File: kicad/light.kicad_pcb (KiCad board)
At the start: 2 copper layers, 166 parts, among them J1 USB_C, J2 SM03B-SRSS-TB, J3 Barrell Jack, J4 01x04, J5 Conn_01x09_MountingPin, J6 01x04, SW1 Boot, SW2 Reset, SW3 On/Off, SW4 Mode, SW5 RotaryEncoder_Switch_MP, U1 RP2350A-QFN60, U2 TPS5405DR, U3 W25Q128JVS, U4 LBEE5KL1YN-814, U5 TPS2115ADRBR, U6 TPS2115ADRBR, U7 HDC1080, U8 MAX6818EAP_T, U9 PIR223D-S0, Y1 ABM8-272-T3

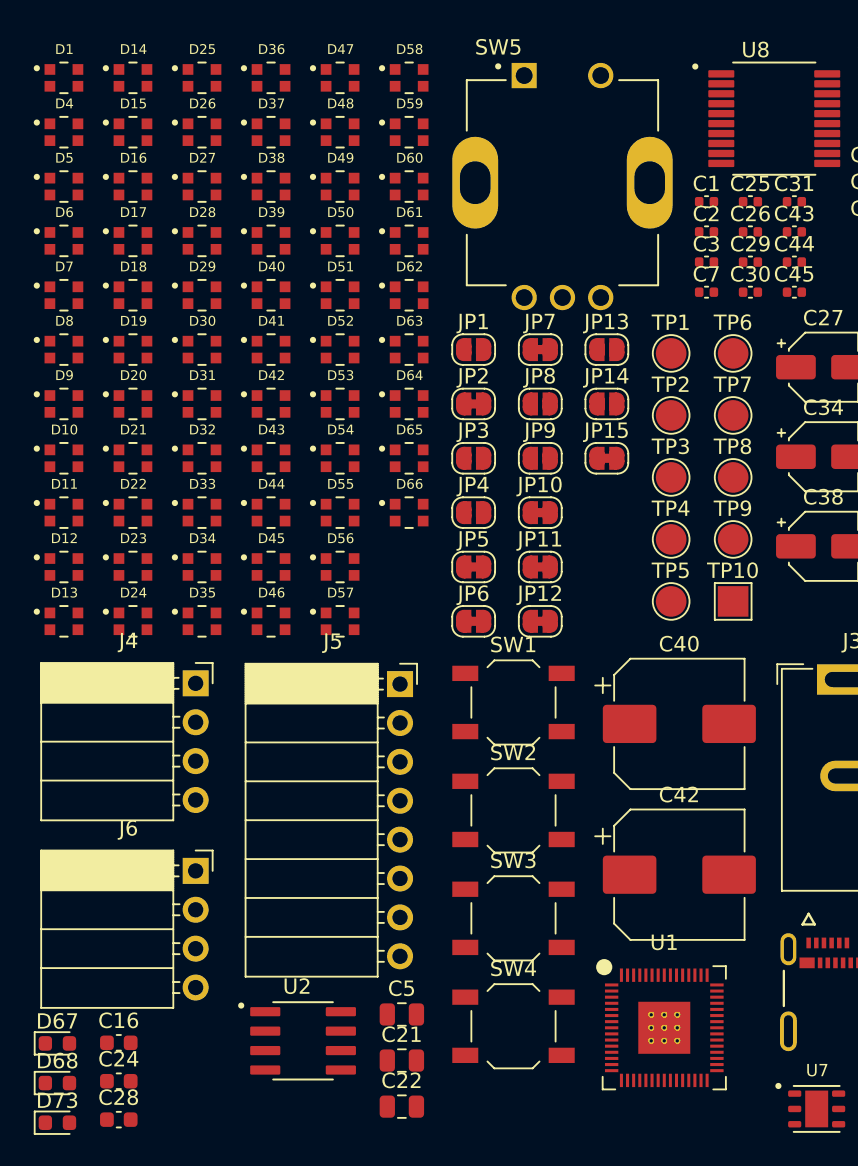
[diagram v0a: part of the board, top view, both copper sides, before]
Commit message: set inductors
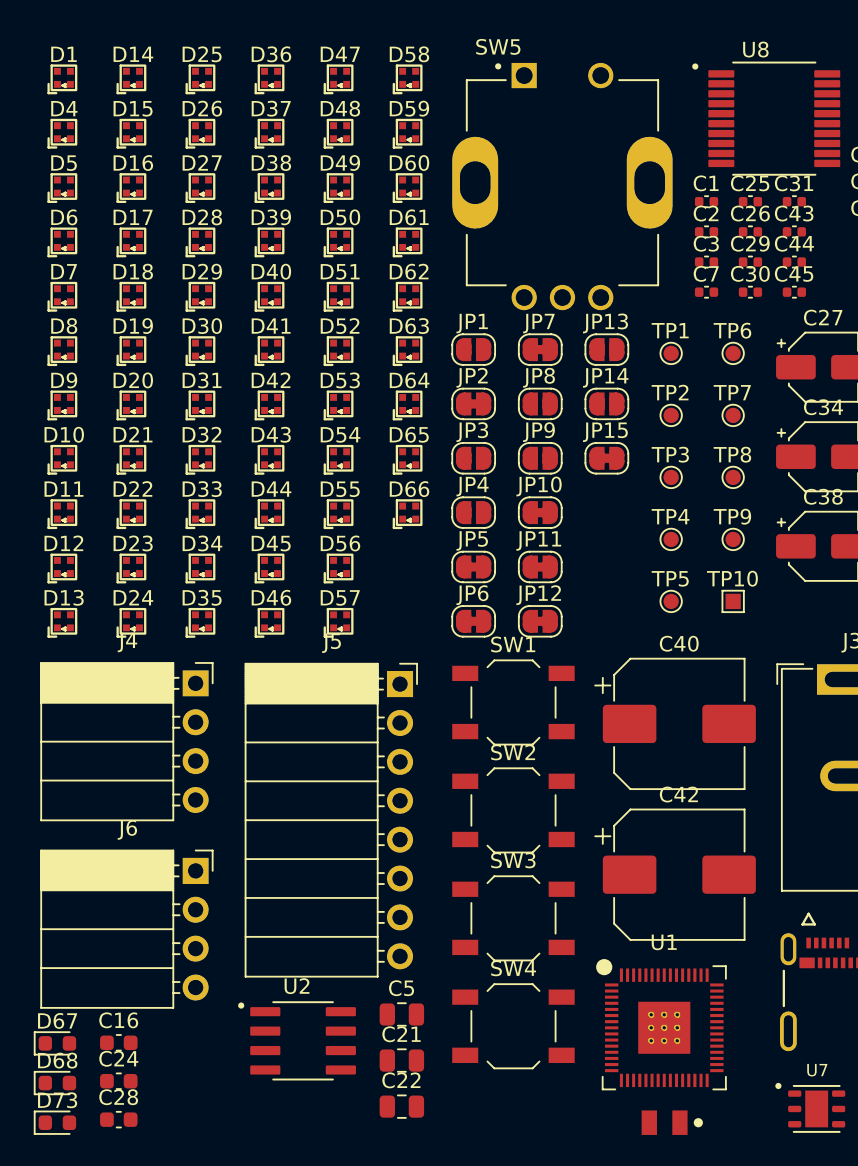
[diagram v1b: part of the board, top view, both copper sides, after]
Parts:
- added L1: 3.3u, AOTA-B201610S3R3-101-T:AOTA-B201610S3R3-101-T, F.Cu at (153.2, 129.8)
- D1, D10, D11, D12, D13, D14, D15, D16, D17, D18, D19, D20, D21, D22, D23, D24, D25, D26, D27, D28, D29, D30, D31, D32, D33, D34, D35, D36, D37, D38, D39, D4, D40, D41, D42, D43, D44, D45, D46, D47, D48, D49, D5, D50, D51, D52, D53, D54, D55, D56, D57, D58, D59, D6, D60, D61, D62, D63, D64, D65, D66, D7, D8, D9: footprint WS2812B_1010:WS2812C-2020 -> WS2812B_1010:WS2812B_1010
- TP1, TP5, TP6, TP7, TP8, TP9: footprint TestPoint:TestPoint_Pad_D2.0mm -> TestPoint:TestPoint_Pad_D1.0mm
- TP10: footprint TestPoint:TestPoint_Pad_2.0x2.0mm -> TestPoint:TestPoint_Pad_1.0x1.0mm
- TP2: value TestPoint -> D+; footprint TestPoint:TestPoint_Pad_D2.0mm -> TestPoint:TestPoint_Pad_D1.0mm
- TP3: value TestPoint -> D-; footprint TestPoint:TestPoint_Pad_D2.0mm -> TestPoint:TestPoint_Pad_D1.0mm
- TP4: value TestPoint -> GND; footprint TestPoint:TestPoint_Pad_D2.0mm -> TestPoint:TestPoint_Pad_D1.0mm

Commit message: finish footprint selection
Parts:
- removed J7: ~, Connector_JST:JST_SH_SM03B-SRSS-TB_1x03-1MP_P1.00mm_Horizontal
- added J8: ~, Connector_PinSocket_2.54mm:PinSocket_1x03_P2.54mm_Vertical, F.Cu at (104.7, 88.5)
- added J9: Conn_01x09_MountingPin, Connector_PinSocket_2.54mm:PinSocket_1x09_P2.54mm_Vertical, F.Cu at (98.5, 87.0)
- added L3: 4.7u, LQH5BPZ4R7NT0L:LQH5BPZ4R7NT0L_5x5mm, F.Cu at (105.2, 72.2)
- added L4: 2.2u, Inductor_SMD:L_0603_1608Metric, F.Cu at (103.7, 76.8)
- added Q1: NMOS, Package_TO_SOT_SMD:SOT-23, F.Cu at (99.3, 71.3)
- added Q2: NMOS, Package_TO_SOT_SMD:SOT-23, F.Cu at (99.3, 76.0)
- added Q3: NMOS, Package_TO_SOT_SMD:SOT-23, F.Cu at (99.3, 80.6)
- added R1: 33, Resistor_SMD:R_0603_1608Metric, F.Cu at (102.3, 121.5)
- added R10: 27, Resistor_SMD:R_0201_0603Metric, F.Cu at (104.7, 125.0)
- added R11: 1k, Resistor_SMD:R_0402_1005Metric, F.Cu at (104.7, 126.8)
- added R12: 100K, Resistor_SMD:R_0402_1005Metric_Pad0.72x0.64mm_HandSolder, F.Cu at (107.2, 121.5)
- added R13: 100K, Resistor_SMD:R_0201_0603Metric, F.Cu at (107.2, 123.2)
- added R14: 560K, Resistor_SMD:R_0201_0603Metric, F.Cu at (107.2, 125.0)
- added R15: 100K, Resistor_SMD:R_0201_0603Metric, F.Cu at (107.2, 126.8)
- added R16: 27, Resistor_SMD:R_0402_1005Metric, F.Cu at (96.7, 114.1)
- added R17: 15k, Resistor_SMD:R_0402_1005Metric, F.Cu at (96.7, 116.1)
- added R18: 470, Resistor_SMD:R_0402_1005Metric, F.Cu at (96.7, 118.1)
- added R19: 10K, Resistor_SMD:R_0402_1005Metric, F.Cu at (96.7, 120.1)
- added R2: 5.1K, Resistor_SMD:R_0201_0603Metric, F.Cu at (102.3, 123.2)
- added R20: 10K, Resistor_SMD:R_0402_1005Metric, F.Cu at (96.7, 122.0)
- added R21: 5.6K, Resistor_SMD:R_0402_1005Metric, F.Cu at (96.7, 124.0)
- added R22: 10K, Resistor_SMD:R_0402_1005Metric, F.Cu at (99.6, 114.1)
- added R23: 100K, Resistor_SMD:R_0402_1005Metric, F.Cu at (99.6, 116.1)
- added R24: 10K, Resistor_SMD:R_0402_1005Metric, F.Cu at (99.6, 118.1)
- added R25: 100K, Resistor_SMD:R_0402_1005Metric, F.Cu at (99.6, 120.1)
- added R26: 820, Resistor_SMD:R_0402_1005Metric, F.Cu at (99.6, 122.0)
- added R27: 10K, Capacitor_SMD:C_0402_1005Metric, F.Cu at (100.3, 130.1)
- added R28: 10K, Capacitor_SMD:C_0402_1005Metric, F.Cu at (100.3, 132.0)
- added R29: 10K, Capacitor_SMD:C_0402_1005Metric, F.Cu at (100.3, 134.0)
- added R3: 5.1K, Resistor_SMD:R_0201_0603Metric, F.Cu at (102.3, 125.0)
- added R30: 470, Capacitor_SMD:C_0402_1005Metric, F.Cu at (103.2, 130.1)
- added R31: 470, Capacitor_SMD:C_0402_1005Metric, F.Cu at (103.2, 132.0)
- added R32: 470, Capacitor_SMD:C_0402_1005Metric, F.Cu at (103.2, 134.0)
- added R33: 10K, Capacitor_SMD:C_0402_1005Metric, F.Cu at (106.0, 130.1)
- added R34: 100K, Capacitor_SMD:C_0402_1005Metric, F.Cu at (106.0, 132.0)
- added R35: 820, Capacitor_SMD:C_0402_1005Metric, F.Cu at (106.0, 134.0)
- added R36: 4.7K, Resistor_SMD:R_0201_0603Metric, F.Cu at (100.1, 135.9)
- added R37: 4.7K, Resistor_SMD:R_0201_0603Metric, F.Cu at (100.1, 137.6)
- added R4: 330, Resistor_SMD:R_0201_0603Metric, F.Cu at (103.0, 114.3)
- added R40: 10k, Resistor_SMD:R_0402_1005Metric, F.Cu at (97.4, 130.1)
- added R41: 10k, Resistor_SMD:R_0402_1005Metric, F.Cu at (97.4, 132.1)
- added R43: 470, Resistor_SMD:R_0402_1005Metric, F.Cu at (97.4, 134.1)
- added R44: 120, Resistor_SMD:R_0402_1005Metric, F.Cu at (97.4, 136.0)
- added R5: 1.8K, Resistor_SMD:R_0402_1005Metric, F.Cu at (103.0, 116.9)
- added R6: 330, Resistor_SMD:R_0201_0603Metric, F.Cu at (103.0, 119.4)
- added R7: 1k, Resistor_SMD:R_0402_1005Metric, F.Cu at (102.3, 126.8)
- added R8: 1k, Resistor_SMD:R_0201_0603Metric, F.Cu at (104.7, 121.5)
- added R9: 27, Resistor_SMD:R_0201_0603Metric, F.Cu at (104.7, 123.2)
- C34, C38: footprint Capacitor_SMD:CP_Elec_4x5.4 -> Capacitor_SMD:C_0603_1608Metric
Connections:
- L1 pad 1: +1V1 -> /VREG_LX
- L1 pad 2: /VREG_LX -> +1V1

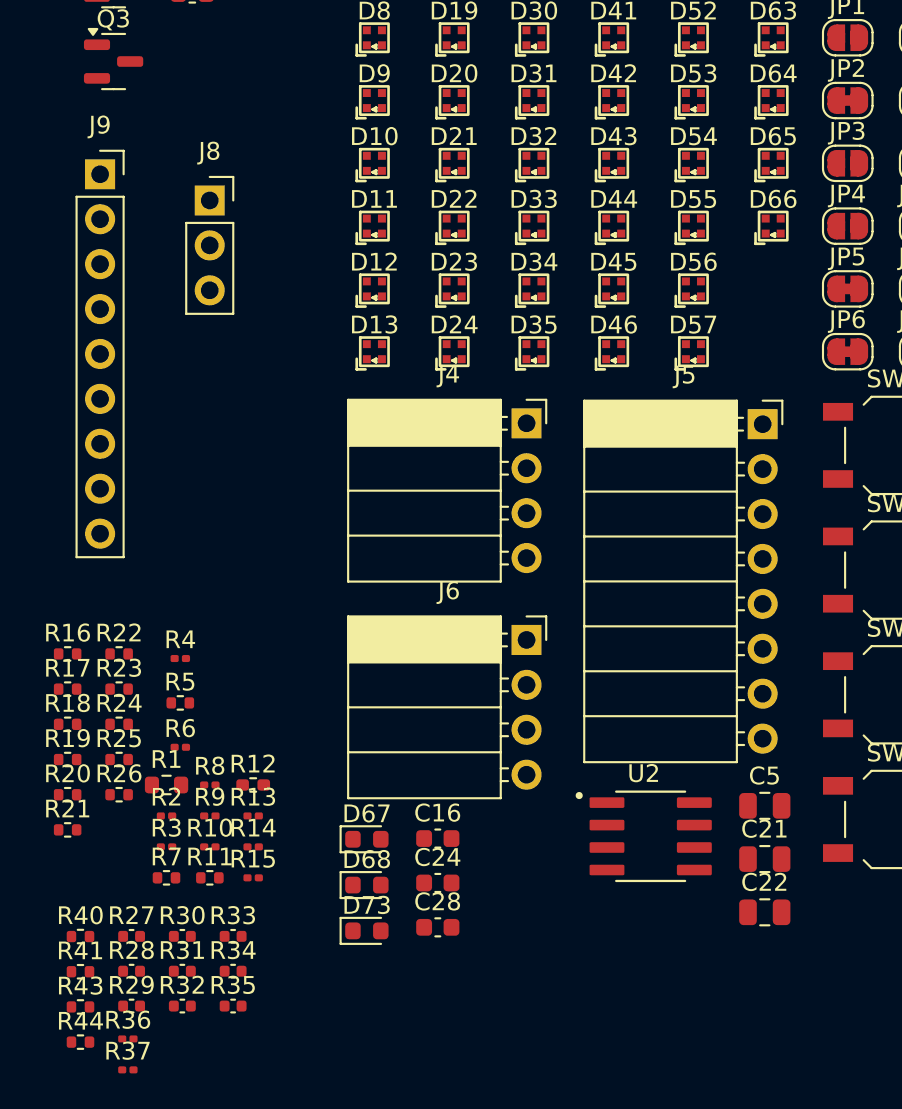
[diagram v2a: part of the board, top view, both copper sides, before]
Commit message: fix wrong pin name on footprints
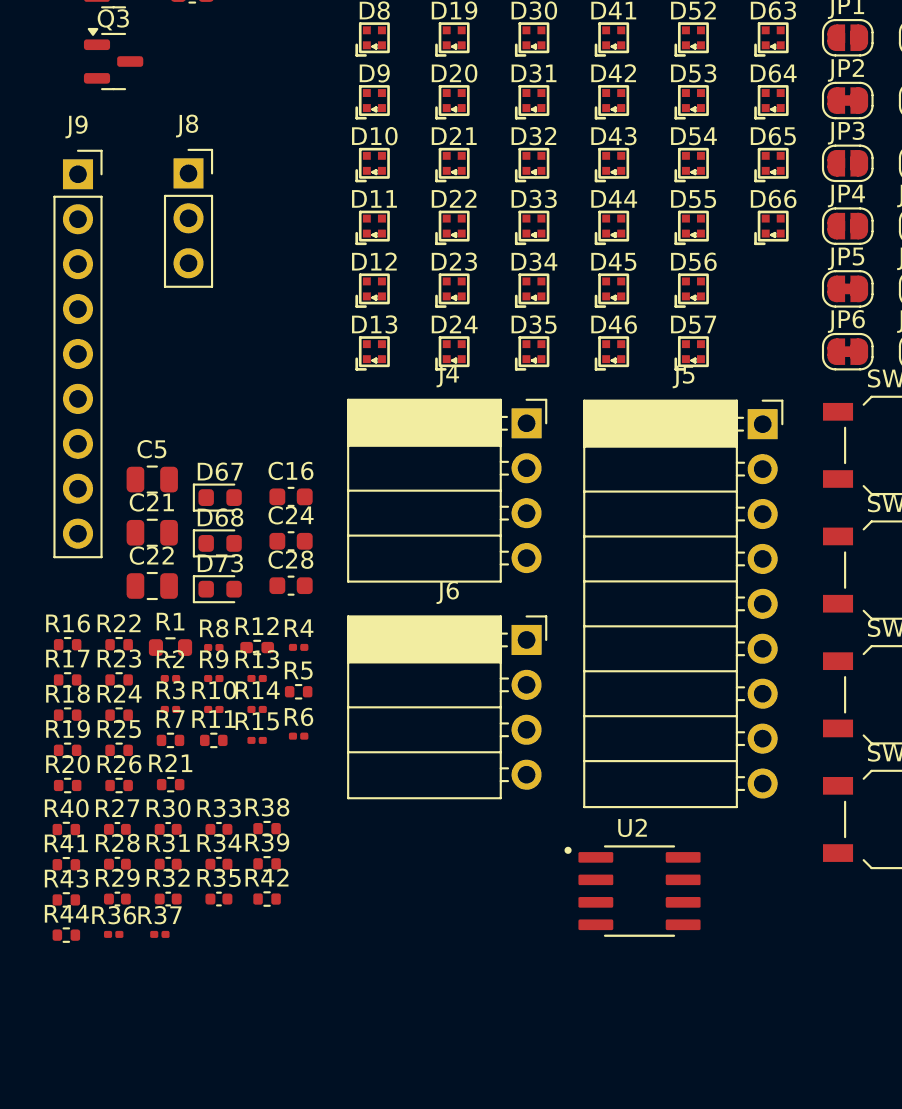
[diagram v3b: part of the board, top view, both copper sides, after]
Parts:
- added R38: 10k, Resistor_SMD:R_0402_1005Metric, F.Cu at (107.9, 124.0)
- added R39: 10k, Resistor_SMD:R_0402_1005Metric, F.Cu at (107.9, 126.0)
- added R42: 10k, Resistor_SMD:R_0402_1005Metric, F.Cu at (107.9, 128.0)
- J5: footprint Connector_PinSocket_2.54mm:PinSocket_1x08_P2.54mm_Horizontal -> Connector_PinSocket_2.54mm:PinSocket_1x09_P2.54mm_Horizontal
- moved C21 39.2 mm to (101.5, 107.2)
- moved C22 39.2 mm to (101.5, 110.2)
- moved C5 39.2 mm to (101.5, 104.2)
- moved C16 21.0 mm to (109.3, 105.2)
- moved C24 21.0 mm to (109.3, 107.7)
- moved C28 21.0 mm to (109.3, 110.2)
- moved D67 21.0 mm to (105.3, 105.2)
- moved D68 21.0 mm to (105.3, 107.8)
- moved D73 21.0 mm to (105.3, 110.4)
- moved R37 7.87 mm to (101.9, 129.9)
- moved R1 7.77 mm to (102.5, 113.7)
- moved R10 7.77 mm to (104.9, 117.2)
- moved R11 7.77 mm to (104.9, 119.0)
- moved R2 7.77 mm to (102.5, 115.5)
- moved R3 7.77 mm to (102.5, 117.2)
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
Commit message: import jlcpcb board settings
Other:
- copper layers 2 -> 4
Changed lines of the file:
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@@
 	(generator_version "9.0")
 	(general
-		(thickness 1.6)
+		(thickness 1.600198)
 		(legacy_teardrops no)
 	)
@@
 	(layers
 		(0 "F.Cu" signal)
+		(4 "In1.Cu" signal)
+		(6 "In2.Cu" signal)
 		(2 "B.Cu" signal)
-		(9 "F.Adhes" user "F.Adhesive")
-		(11 "B.Adhes" user "B.Adhesive")
 		(13 "F.Paste" user)
 		(15 "B.Paste" user)
@@
 		(1 "F.Mask" user)
 		(3 "B.Mask" user)
-		(17 "Dwgs.User" user "User.Drawings")
-		(19 "Cmts.User" user "User.Comments")
-		(21 "Eco1.User" user "User.Eco1")
-		(23 "Eco2.User" user "User.Eco2")
 		(25 "Edge.Cuts" user)
 		(27 "Margin" user)
@@
 		(29 "B.CrtYd" user "B.Courtyard")
 		(35 "F.Fab" user)
-		(33 "B.Fab" user)
-		(39 "User.1" user)
-		(41 "User.2" user)
-		(43 "User.3" user)
-		(45 "User.4" user)
 	)
 	(setup
+		(stackup
+			(layer "F.SilkS"
+				(type "Top Silk Screen")
+			)
+			(layer "F.Paste"
+				(type "Top Solder Paste")
+			)
+			(layer "F.Mask"
+				(type "Top Solder Mask")
+				(thickness 0.01)
+			)
+			(layer "F.Cu"
+				(type "copper")
+				(thickness 0.035)
+			)
+			(layer "dielectric 1"
+				(type "core")
+				(thickness 0.480066)
+				(material "FR4")
+				(epsilon_r 4.5)
+				(loss_tangent 0.02)
+			)
+			(layer "In1.Cu"
+				(type "copper")
+				(thickness 0.035)
+			)
+			(layer "dielectric 2"
+				(type "prepreg")
+				(thickness 0.480066)
+				(material "FR4")
+				(epsilon_r 4.5)
+				(loss_tangent 0.02)
+			)
+			(layer "In2.Cu"
+				(type "copper")
+				(thickness 0.035)
+			)
+			(layer "dielectric 3"
+				(type "core")
+				(thickness 0.480066)
+				(material "FR4")
+				(epsilon_r 4.5)
+				(loss_tangent 0.02)
+			)
+			(layer "B.Cu"
+				(type "copper")
+				(thickness 0.035)
+			)
+			(layer "B.Mask"
+				(type "Bottom Solder Mask")
+				(thickness 0.01)
+			)
+			(layer "B.Paste"
+				(type "Bottom Solder Paste")
+			)
+			(layer "B.SilkS"
+				(type "Bottom Silk Screen")
+			)
+			(copper_finish "None")
+			(dielectric_constraints no)
+		)
 		(pad_to_mask_clearance 0)
+		(solder_mask_min_width 0.1016)
 		(allow_soldermask_bridges_in_footprints no)
 		(tenting front back)

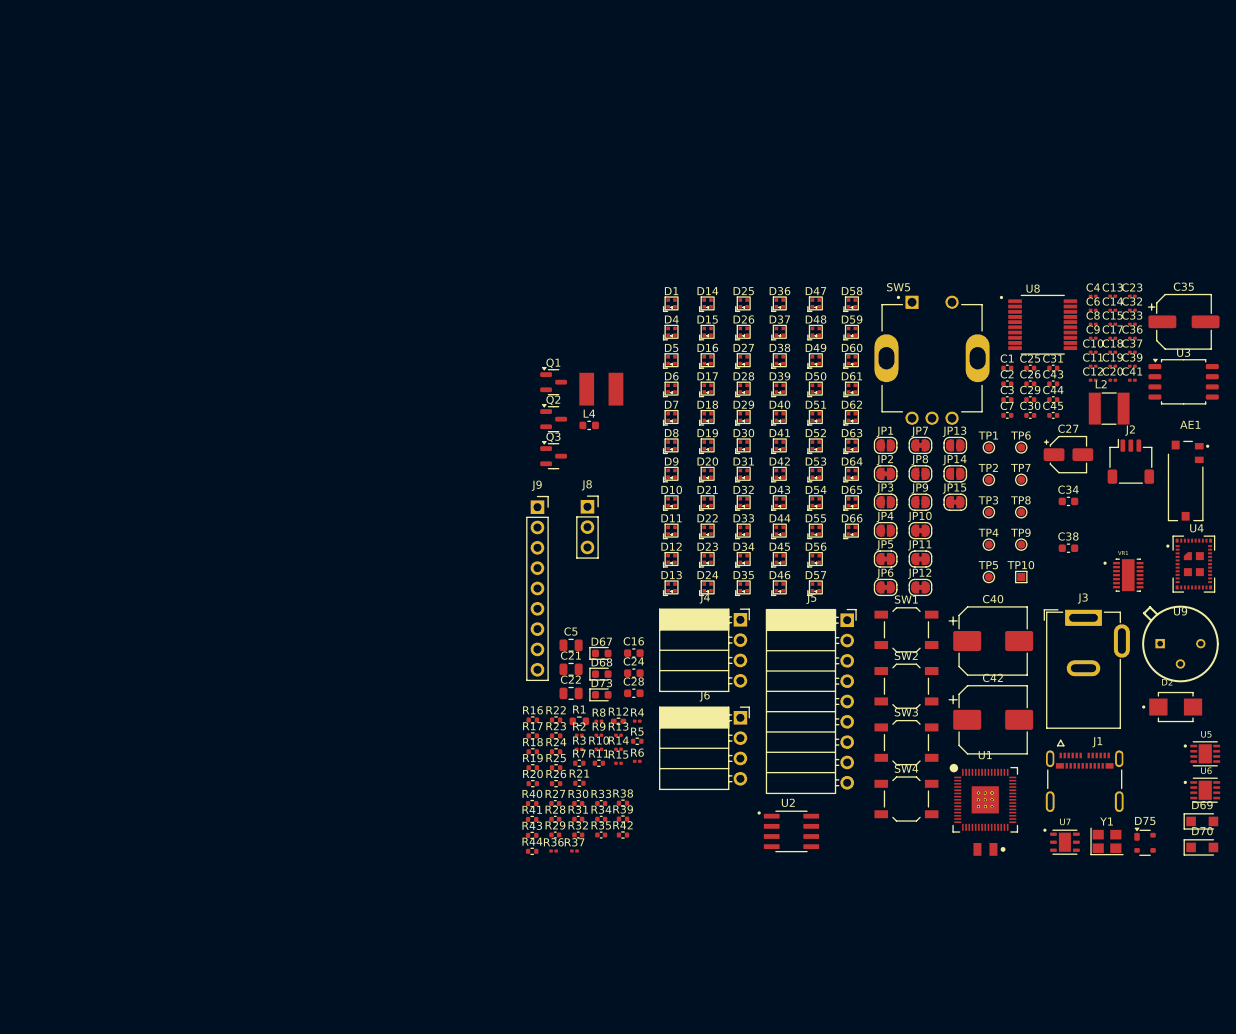
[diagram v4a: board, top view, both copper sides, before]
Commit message: group components
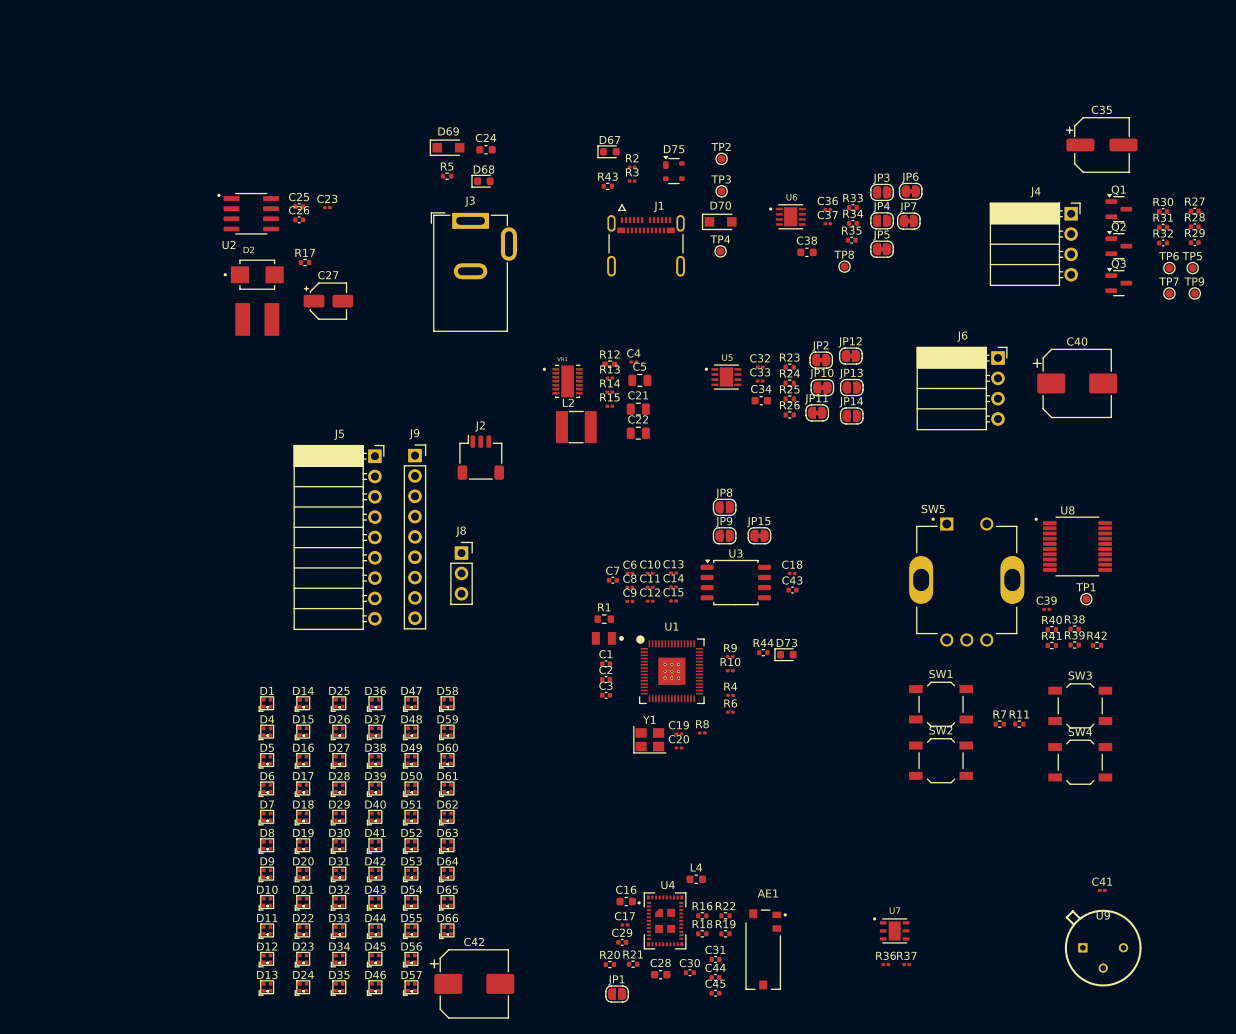
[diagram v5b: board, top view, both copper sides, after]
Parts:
- removed TP10: GND, TestPoint:TestPoint_Pad_1.0x1.0mm
- moved D2 126.9 mm to (62.2, 57.9)
- moved D69 126.4 mm to (86.1, 42.0)
- moved R27 109.0 mm to (179.4, 50.0)
- moved R28 109.0 mm to (179.4, 51.9)
- moved R29 109.0 mm to (179.4, 53.9)
- moved R30 104.0 mm to (175.5, 50.0)
- moved R31 104.0 mm to (175.5, 52.0)
- moved R32 104.0 mm to (175.5, 54.0)
- moved U2 102.6 mm to (61.5, 50.3)
- moved D75 102.6 mm to (114.3, 45.0)
- moved C23 101.2 mm to (71.0, 49.5)
- moved D70 98.7 mm to (120.1, 51.3)
- moved C17 95.4 mm to (108.2, 139.2)
- moved C27 94.5 mm to (71.1, 61.2)
- moved C26 93.7 mm to (67.5, 51.1)
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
